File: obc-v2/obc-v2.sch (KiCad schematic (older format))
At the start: 12 parts

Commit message: obc-v2: Update microcontroller power circuitry
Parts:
- removed C? (x2): 15pF, symbol Device:C
- removed R?: R_US, symbol Device:R_US
- added FB?: Ferrite_Bead, symbol Device:Ferrite_Bead
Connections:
- net labels removed: AIN1, AIN2, AIN3, INT3, INT4, VOUT, XOUT
- wire segments 40 -> 32
- no-connect marks 0 -> 2
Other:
- moved on the sheet: C?

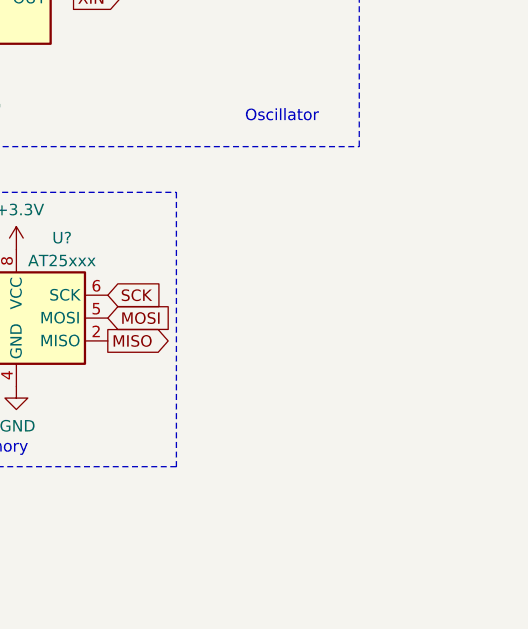
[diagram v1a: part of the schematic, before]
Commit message: obc-v2: Add BMI088 symbol
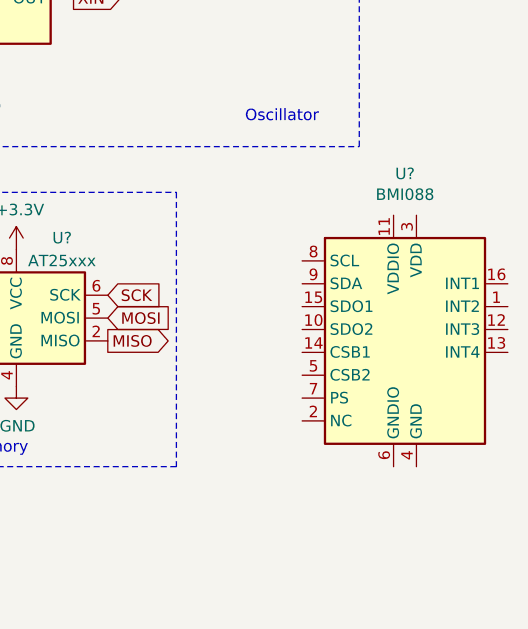
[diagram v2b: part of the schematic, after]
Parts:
- added U?: BMI088, Package_LGA:Bosch_LGA-14_3x2.5mm_P0.5mm, symbol bmi088:BMI088
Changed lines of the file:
@@
 Wire Notes Line
 	4150 800  4150 4550
+$Comp
+L bmi088:BMI088 U?
+U 1 1 6126D77D
+P 7250 2700
+F 0 "U?" H 7200 3281 50  0000 C CNN
+F 1 "BMI088" H 7200 3190 50  0000 C CNN
+F 2 "Package_LGA:Bosch_LGA-14_3x2.5mm_P0.5mm" H 7250 2700 50  0001 C CNN
+F 3 "https://ae-bst.resource.bosch.com/media/_tech/media/datasheets/BST-BMI160-DS000.pdf" H 6550 3550 50  0001 C CNN
+	1    7250 2700
+	1    0    0    -1
+$EndComp
 $EndSCHEMATC

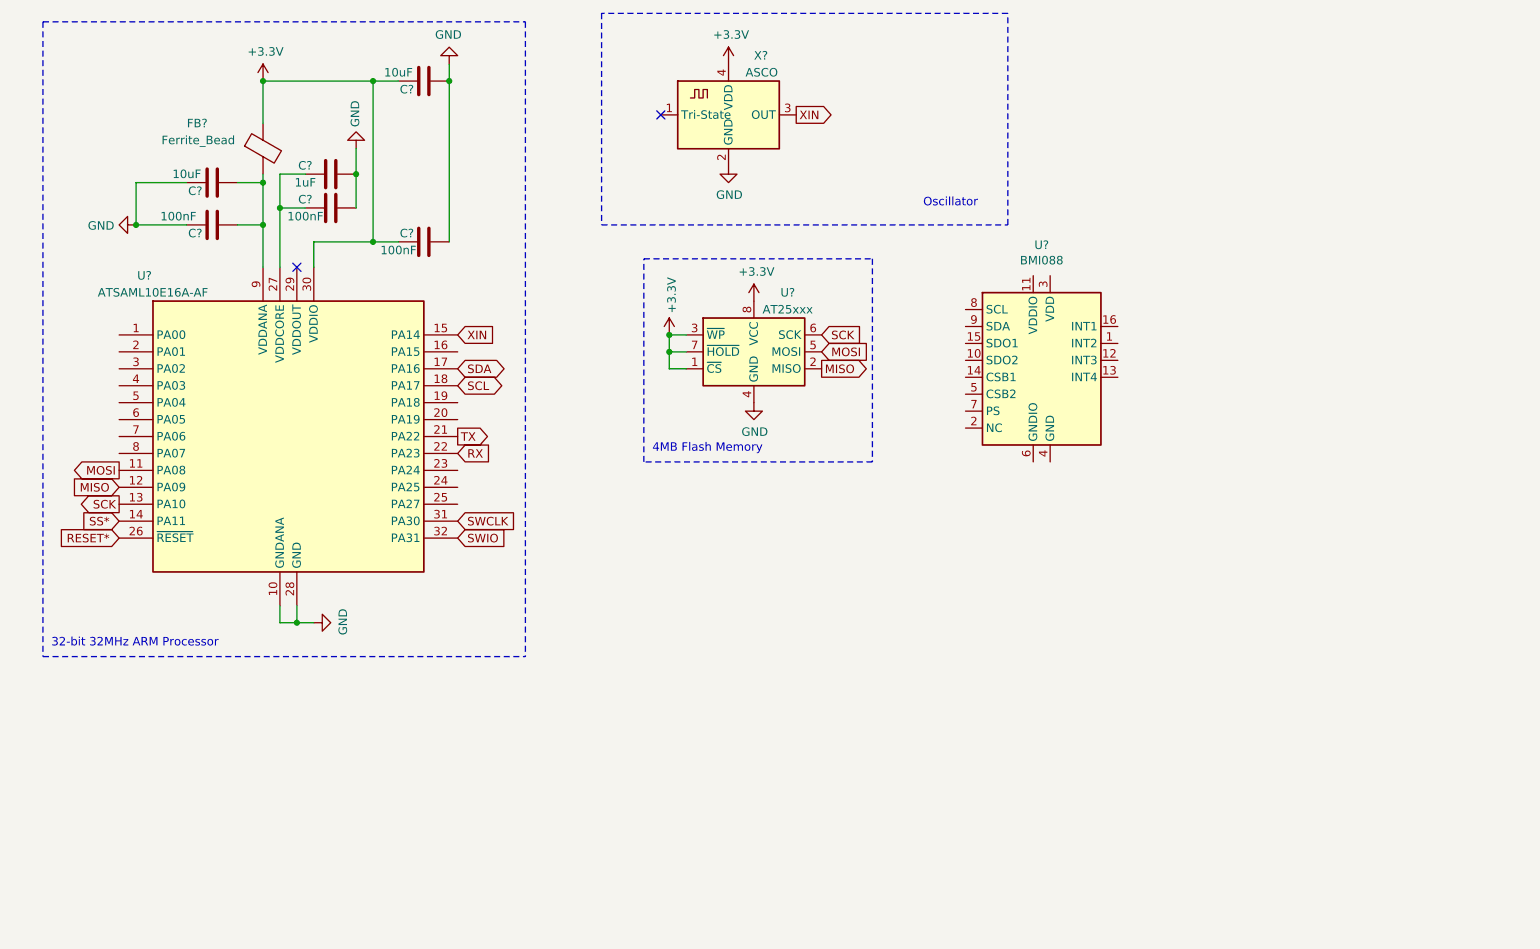
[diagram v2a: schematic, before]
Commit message: obc-v2: Add IMU
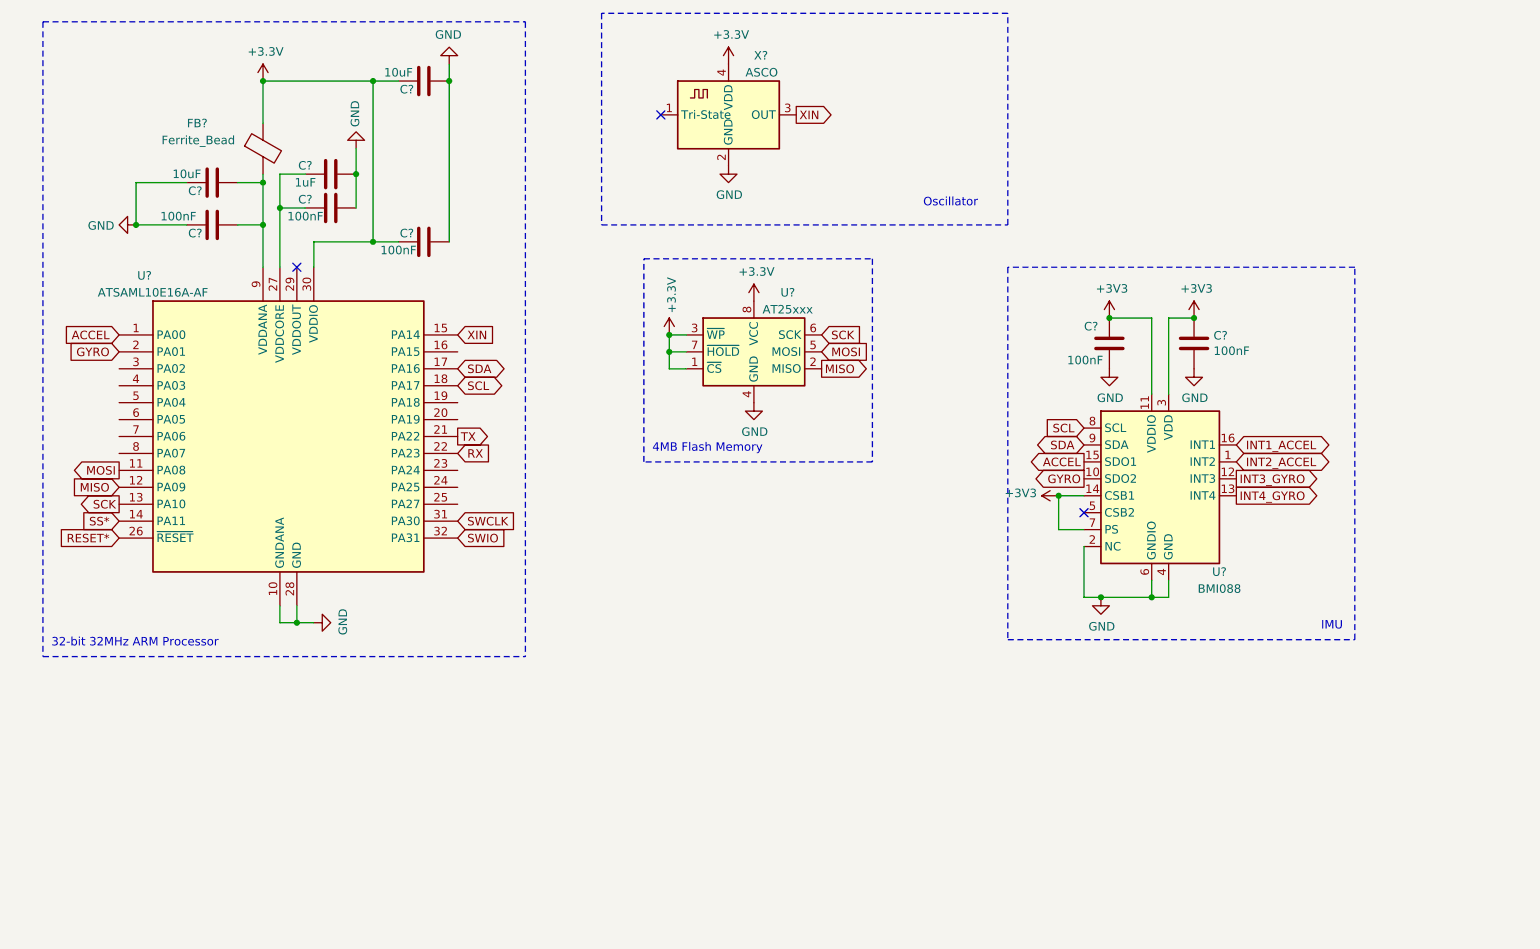
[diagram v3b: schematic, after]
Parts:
- added C? (x2): 100nF, symbol Device:C
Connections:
- net +3V3: now also U?.11 (VDDIO), U?.14 (CSB1), U?.3 (VDD), U?.7 (PS), C?.1, C?.1
- net GND: now also U?.2 (NC), U?.4 (GND), U?.6 (GNDIO), C?.2, C?.2
- net SCL: now also U?.8 (SCL)
- net SDA: now also U?.9 (SDA)
- net ACCEL: now reaches U?.1 (PA00)
- net ACCEL: now also U?.15 (SDO1)
- net GYRO: now reaches U?.2 (PA01)
- net GYRO: now also U?.10 (SDO2)
- net INT2_ACCEL: now reaches U?.1 (INT2)
- net INT3_GYRO: now reaches U?.12 (INT3)
- net INT4_GYRO: now reaches U?.13 (INT4)
- net INT1_ACCEL: now reaches U?.16 (INT1)
- no-connect marks 2 -> 3
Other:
- note added: "IMU"
- moved on the sheet: U?
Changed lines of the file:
@@
 Wire Notes Line
 	4150 800  4150 4550
+Text GLabel 7450 3300 0    50   BiDi ~ 0
+SDA
+Text GLabel 7450 3200 0    50   Input ~ 0
+SCL
+Text GLabel 7450 3400 0    50   Output ~ 0
+ACCEL
+Text GLabel 7450 3500 0    50   Output ~ 0
+GYRO
+NoConn ~ 7450 3700
+$Comp
+L power:GND #PWR?
+U 1 1 612718CF
+P 7550 4200
+F 0 "#PWR?" H 7550 3950 50  0001 C CNN
+F 1 "GND" H 7555 4027 50  0000 C CNN
+F 2 "" H 7550 4200 50  0001 C CNN
+F 3 "" H 7550 4200 50  0001 C CNN
+	1    7550 4200
+	1    0    0    -1
+$EndComp
+Wire Wire Line
+	7450 3900 7450 4200
+Wire Wire Line
+	7450 4200 7550 4200
+Wire Wire Line
+	7950 4200 7950 4100
+Connection ~ 7550 4200
+Wire Wire Line
+	7550 4200 7850 4200
+Wire Wire Line
+	7850 4100 7850 4200
+Connection ~ 7850 4200
+Wire Wire Line
+	7850 4200 7950 4200
+$Comp
+L power:+3V3 #PWR?
+U 1 1 61272ED0
+P 7300 3600
+F 0 "#PWR?" H 7300 3450 50  0001 C CNN
+F 1 "+3V3" V 7315 3728 50  0000 L CNN
+F 2 "" H 7300 3600 50  0001 C CNN
+F 3 "" H 7300 3600 50  0001 C CNN
+	1    7300 3600
+	0    -1   -1   0
+$EndComp
+Wire Wire Line
+	7450 3600 7300 3600
+Wire Wire Line
+	7300 3600 7300 3800
+Wire Wire Line
+	7300 3800 7450 3800
+Connection ~ 7300 3600
+Text GLabel 8350 3300 2    50   BiDi ~ 0
+INT1_ACCEL
+Text GLabel 8350 3400 2    50   BiDi ~ 0
+INT2_ACCEL
 $Comp
 L bmi088:BMI088 U?
 U 1 1 6126D77D
-P 7250 2700
-F 0 "U?" H 7200 3281 50  0000 C CNN
-F 1 "BMI088" H 7200 3190 50  0000 C CNN
-F 2 "Package_LGA:Bosch_LGA-14_3x2.5mm_P0.5mm" H 7250 2700 50  0001 C CNN
-F 3 "https://ae-bst.resource.bosch.com/media/_tech/media/datasheets/BST-BMI160-DS000.pdf" H 6550 3550 50  0001 C CNN
-	1    7250 2700
+P 7950 3400
+F 0 "U?" H 8250 2750 50  0000 C CNN
+F 1 "BMI088" H 8250 2650 50  0000 C CNN
+F 2 "Package_LGA:Bosch_LGA-14_3x2.5mm_P0.5mm" H 7950 3400 50  0001 C CNN
+F 3 "https://ae-bst.resource.bosch.com/media/_tech/media/datasheets/BST-BMI160-DS000.pdf" H 7250 4250 50  0001 C CNN
+	1    7950 3400
 	1    0    0    -1
 $EndComp
+Text GLabel 8350 3500 2    50   Output ~ 0
+INT3_GYRO
+Text GLabel 8350 3600 2    50   Output ~ 0
+INT4_GYRO
+$Comp
+L power:+3V3 #PWR?
+U 1 1 61277D25
+P 7600 2550
+F 0 "#PWR?" H 7600 2400 50  0001 C CNN
+F 1 "+3V3" H 7615 2723 50  0000 C CNN
+F 2 "" H 7600 2550 50  0001 C CNN
+F 3 "" H 7600 2550 50  0001 C CNN
+	1    7600 2550
+	1    0    0    -1
+$EndComp
+$Comp
+L power:+3V3 #PWR?
+U 1 1 612781FE
+P 8100 2550
+F 0 "#PWR?" H 8100 2400 50  0001 C CNN
+F 1 "+3V3" H 8115 2723 50  0000 C CNN
+F 2 "" H 8100 2550 50  0001 C CNN
+F 3 "" H 8100 2550 50  0001 C CNN
+	1    8100 2550
+	1    0    0    -1
+$EndComp
+$Comp
+L Device:C C?
+U 1 1 612799A4
+P 7600 2700
+F 0 "C?" H 7450 2800 50  0000 L CNN
+F 1 "100nF" H 7350 2600 50  0000 L CNN
+F 2 "" H 7638 2550 50  0001 C CNN
+F 3 "~" H 7600 2700 50  0001 C CNN
+	1    7600 2700
+	1    0    0    -1
+$EndComp
+$Comp
+L Device:C C?
+U 1 1 6127A006
+P 8100 2700
+F 0 "C?" H 8215 2746 50  0000 L CNN
+F 1 "100nF" H 8215 2655 50  0000 L CNN
+F 2 "" H 8138 2550 50  0001 C CNN
+F 3 "~" H 8100 2700 50  0001 C CNN
+	1    8100 2700
+	1    0    0    -1
+$EndComp
+$Comp
+L power:GND #PWR?
+U 1 1 6127AE14
+P 7600 2850
+F 0 "#PWR?" H 7600 2600 50  0001 C CNN
+F 1 "GND" H 7605 2677 50  0000 C CNN
+F 2 "" H 7600 2850 50  0001 C CNN
+F 3 "" H 7600 2850 50  0001 C CNN
+	1    7600 2850
+	1    0    0    -1
+$EndComp
+$Comp
+L power:GND #PWR?
+U 1 1 6127B677
+P 8100 2850
+F 0 "#PWR?" H 8100 2600 50  0001 C CNN
+F 1 "GND" H 8105 2677 50  0000 C CNN
+F 2 "" H 8100 2850 50  0001 C CNN
+F 3 "" H 8100 2850 50  0001 C CNN
+	1    8100 2850
+	1    0    0    -1
+$EndComp
+Wire Wire Line
+	7600 2550 7850 2550
+Wire Wire Line
+	7850 2550 7850 3000
+Connection ~ 7600 2550
+Wire Wire Line
+	8100 2550 7950 2550
+Wire Wire Line
+	7950 2550 7950 3000
+Connection ~ 8100 2550
+Wire Notes Line
+	7000 2250 7000 4450
+Wire Notes Line
+	7000 4450 9050 4450
+Wire Notes Line
+	9050 4450 9050 2250
+Wire Notes Line
+	9050 2250 7000 2250
+Text Notes 8850 4400 0    50   ~ 0
+IMU
+Text GLabel 1750 2650 0    50   Input ~ 0
+ACCEL
+Text GLabel 1750 2750 0    50   Input ~ 0
+GYRO
 $EndSCHEMATC

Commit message: obc-v2: Add IMU interrupt and memory chip select connections
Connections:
- net +3V3: now also U?.10 (SDO2), U?.15 (SDO1); no longer U?.1 (~CS)
- net INT1_ACCEL: now also U?.1 (PA00)
- net INT2_ACCEL: now also U?.2 (PA01)
- net INT3_GYRO: now also U?.3 (PA02)
- net INT4_GYRO: now also U?.4 (PA03)
- net SS*: now also U?.1 (~CS)
- removed net ACCEL: U?.1 (PA00), U?.15 (SDO1)
- removed net GYRO: U?.10 (SDO2), U?.2 (PA01)
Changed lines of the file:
@@
 Text GLabel 1750 3650 0    50   Output ~ 0
 SCK
-Text GLabel 1750 3750 0    50   Input ~ 0
+Text GLabel 1750 3750 0    50   Output ~ 0
 SS*
 Text GLabel 1750 3850 0    50   Input ~ 0
@@
 RX
 $Comp
-L MCU_Microchip_SAML_NEW:ATSAML10E16A-AF U?
-U 1 1 61106D2F
-P 2750 3250
-F 0 "U?" H 1900 4200 50  0000 C CNN
-F 1 "ATSAML10E16A-AF" H 1950 4100 50  0000 C CNN
-F 2 "Package_QFP:TQFP-32_7x7mm_P0.8mm" H 3750 4150 50  0001 C CNN
-F 3 "https://ww1.microchip.com/downloads/en/DeviceDoc/SAM-L10L11-Family-DataSheet-DS60001513F.pdf" H 2750 3250 50  0001 C CNN
-	1    2750 3250
-	1    0    0    -1
-$EndComp
-$Comp
 L power:+3.3V #PWR?
 U 1 1 61149F54
@@
 	1    0    0    -1
 $EndComp
-Wire Notes Line
-	1300 800  4150 800
 $Comp
 L power:GND #PWR?
@@
 	5000 2650 5000 2750
 Wire Wire Line
-	5000 2850 5100 2850
-Wire Wire Line
 	5000 2750 5100 2750
-Connection ~ 5000 2750
-Wire Wire Line
-	5000 2750 5000 2850
 Wire Wire Line
 	5000 2650 5100 2650
@@
 	2800 4250 2800 4350
 Wire Notes Line
-	1300 800  1300 4550
-Wire Notes Line
-	1300 4550 4150 4550
+	1200 800  1200 4550
 Wire Notes Line
 	4150 800  4150 4550
@@
 Text GLabel 7450 3200 0    50   Input ~ 0
 SCL
-Text GLabel 7450 3400 0    50   Output ~ 0
-ACCEL
-Text GLabel 7450 3500 0    50   Output ~ 0
-GYRO
 NoConn ~ 7450 3700
 $Comp
@@
 	7300 3800 7450 3800
 Connection ~ 7300 3600
-Text GLabel 8350 3300 2    50   BiDi ~ 0
+Text GLabel 8350 3300 2    50   Output ~ 0
 INT1_ACCEL
-Text GLabel 8350 3400 2    50   BiDi ~ 0
+Text GLabel 8350 3400 2    50   Output ~ 0
 INT2_ACCEL
 $Comp
@@
 Connection ~ 8100 2550
 Wire Notes Line
-	7000 2250 7000 4450
-Wire Notes Line
-	7000 4450 9050 4450
+	6900 2250 6900 4450
 Wire Notes Line
 	9050 4450 9050 2250
-Wire Notes Line
-	9050 2250 7000 2250
 Text Notes 8850 4400 0    50   ~ 0
 IMU
+Wire Wire Line
+	7450 3400 7300 3400
+Wire Wire Line
+	7450 3500 7300 3500
+Wire Wire Line
+	7300 3400 7300 3500
+Connection ~ 7300 3500
+Wire Wire Line
+	7300 3500 7300 3600
 Text GLabel 1750 2650 0    50   Input ~ 0
-ACCEL
+INT1_ACCEL
 Text GLabel 1750 2750 0    50   Input ~ 0
-GYRO
+INT2_ACCEL
+Text GLabel 1750 2850 0    50   Input ~ 0
+INT3_GYRO
+Text GLabel 1750 2950 0    50   Input ~ 0
+INT4_GYRO
+$Comp
+L MCU_Microchip_SAML_NEW:ATSAML10E16A-AF U?
+U 1 1 61106D2F
+P 2750 3250
+F 0 "U?" H 1900 4200 50  0000 C CNN
+F 1 "ATSAML10E16A-AF" H 1950 4100 50  0000 C CNN
+F 2 "Package_QFP:TQFP-32_7x7mm_P0.8mm" H 3750 4150 50  0001 C CNN
+F 3 "https://ww1.microchip.com/downloads/en/DeviceDoc/SAM-L10L11-Family-DataSheet-DS60001513F.pdf" H 2750 3250 50  0001 C CNN
+	1    2750 3250
+	1    0    0    -1
+$EndComp
+Wire Notes Line
+	1200 4550 4150 4550
+Wire Notes Line
+	1200 800  4150 800
+Text GLabel 5100 2850 0    50   Input ~ 0
+SS*
+Wire Notes Line
+	6900 4450 9050 4450
+Wire Notes Line
+	6900 2250 9050 2250
 $EndSCHEMATC

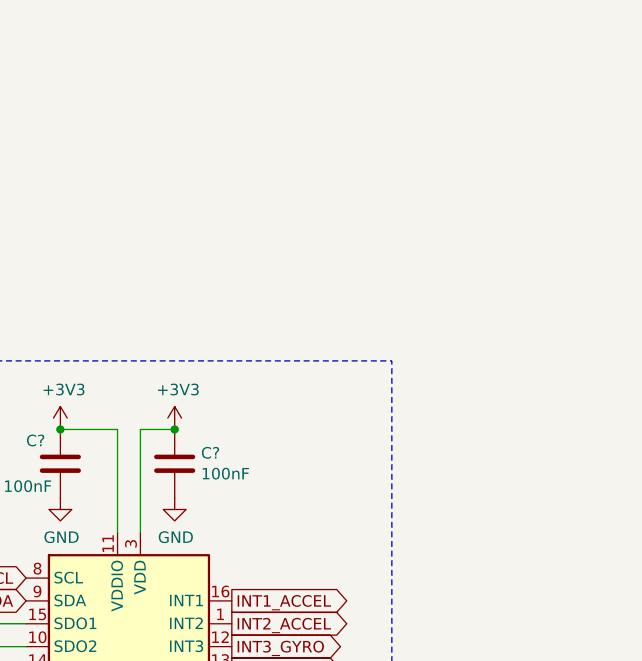
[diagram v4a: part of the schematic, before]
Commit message: obc-v2: Add barometer
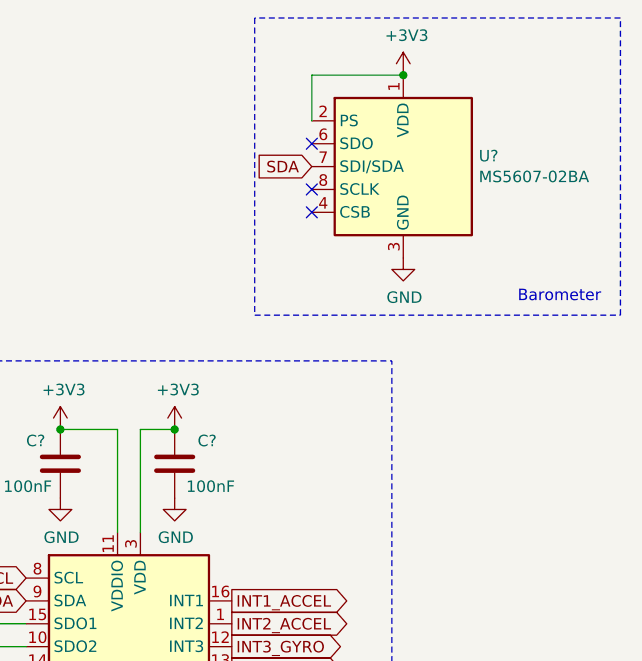
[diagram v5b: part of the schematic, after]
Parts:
- added U?: MS5607-02BA, Package_LGA:LGA-8_3x5mm_P1.25mm, symbol Sensor_Pressure:MS5607-02BA
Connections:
- net +3V3: now also U?.1 (VDD), U?.2 (PS)
- net GND: now also U?.3 (GND)
- net SDA: now also U?.7 (SDI/SDA)
- new net: U?.4 (CSB), U?.5 (CSB)
- no-connect marks 3 -> 6
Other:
- note added: "Barometer"
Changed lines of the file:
@@
 U 1 1 6127A006
 P 8100 2700
-F 0 "C?" H 8215 2746 50  0000 L CNN
-F 1 "100nF" H 8215 2655 50  0000 L CNN
+F 0 "C?" H 8200 2800 50  0000 L CNN
+F 1 "100nF" H 8150 2600 50  0000 L CNN
 F 2 "" H 8138 2550 50  0001 C CNN
 F 3 "~" H 8100 2700 50  0001 C CNN
@@
 Wire Notes Line
 	6900 2250 9050 2250
+$Comp
+L Sensor_Pressure:MS5607-02BA U?
+U 1 1 61291CE6
+P 9100 1400
+F 0 "U?" H 9430 1446 50  0000 L CNN
+F 1 "MS5607-02BA" H 9430 1355 50  0000 L CNN
+F 2 "Package_LGA:LGA-8_3x5mm_P1.25mm" H 9100 1400 50  0001 C CNN
+F 3 "https://www.te.com/commerce/DocumentDelivery/DDEController?Action=showdoc&DocId=Data+Sheet%7FMS5607-02BA03%7FB2%7Fpdf%7FEnglish%7FENG_DS_MS5607-02BA03_B2.pdf%7FCAT-BLPS0035" H 9100 1400 50  0001 C CNN
+	1    9100 1400
+	1    0    0    -1
+$EndComp
+$Comp
+L power:GND #PWR?
+U 1 1 61292644
+P 9100 1800
+F 0 "#PWR?" H 9100 1550 50  0001 C CNN
+F 1 "GND" H 9105 1627 50  0000 C CNN
+F 2 "" H 9100 1800 50  0001 C CNN
+F 3 "" H 9100 1800 50  0001 C CNN
+	1    9100 1800
+	1    0    0    -1
+$EndComp
+$Comp
+L power:+3V3 #PWR?
+U 1 1 61292BCA
+P 9100 1000
+F 0 "#PWR?" H 9100 850 50  0001 C CNN
+F 1 "+3V3" H 9115 1173 50  0000 C CNN
+F 2 "" H 9100 1000 50  0001 C CNN
+F 3 "" H 9100 1000 50  0001 C CNN
+	1    9100 1000
+	1    0    0    -1
+$EndComp
+Wire Wire Line
+	8700 1200 8700 1000
+Wire Wire Line
+	8700 1000 9100 1000
+Connection ~ 9100 1000
+Text GLabel 8700 1400 0    50   Input ~ 0
+SDA
+NoConn ~ 8700 1300
+NoConn ~ 8700 1500
+NoConn ~ 8700 1600
+Wire Notes Line
+	10050 2050 10050 750
+Wire Notes Line
+	10050 750  8450 750
+Wire Notes Line
+	8450 750  8450 2050
+Wire Notes Line
+	8450 2050 10050 2050
+Text Notes 9600 2000 0    50   ~ 0
+Barometer
 $EndSCHEMATC

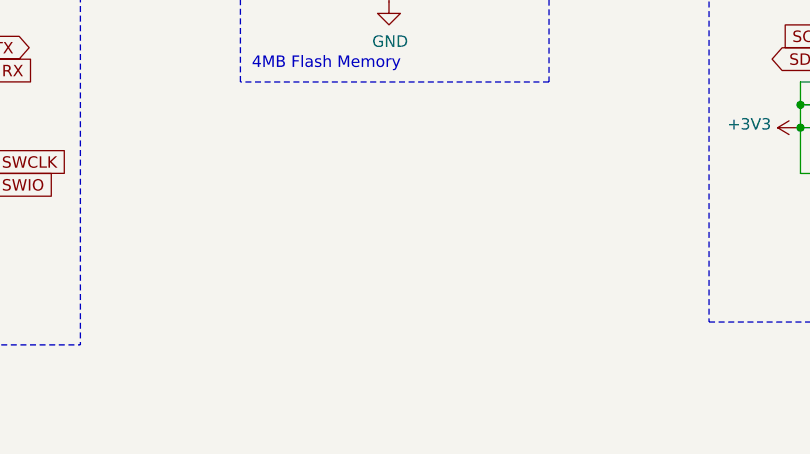
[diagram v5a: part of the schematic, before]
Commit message: Add 1-wire interface for thermal sensors
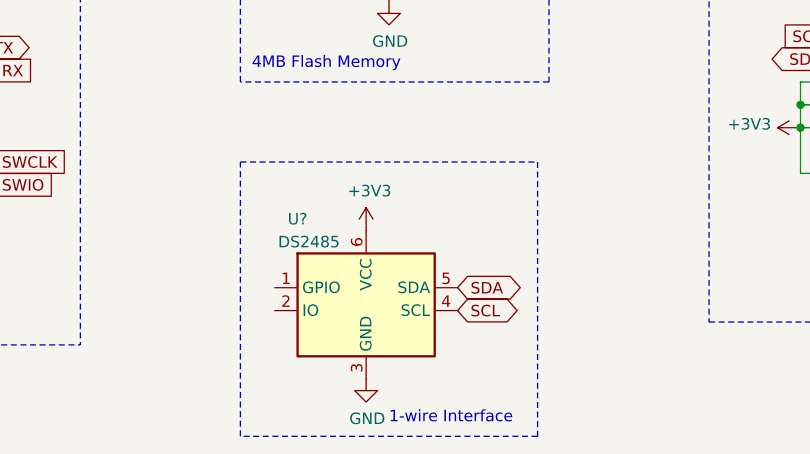
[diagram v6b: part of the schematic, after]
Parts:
- added U?: DS2485, symbol DS2845:DS2485
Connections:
- net +3V3: now also U?.6 (VCC)
- net GND: now also U?.3 (GND)
- net SCL: now also U?.4 (SCL)
- net SDA: now also U?.5 (SDA)
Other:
- note added: "1-wire Interface"
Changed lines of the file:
@@
 Text Notes 9600 2000 0    50   ~ 0
 Barometer
+$Comp
+L DS2845:DS2485 U?
+U 1 1 6129E0CF
+P 5400 4350
+F 0 "U?" H 5100 4700 50  0000 C CNN
+F 1 "DS2485" H 5150 4600 50  0000 C CNN
+F 2 "" H 5450 4500 50  0001 C CNN
+F 3 "" H 5450 4500 50  0001 C CNN
+	1    5400 4350
+	1    0    0    -1
+$EndComp
+$Comp
+L power:GND #PWR?
+U 1 1 6129E849
+P 5400 4700
+F 0 "#PWR?" H 5400 4450 50  0001 C CNN
+F 1 "GND" H 5405 4527 50  0000 C CNN
+F 2 "" H 5400 4700 50  0001 C CNN
+F 3 "" H 5400 4700 50  0001 C CNN
+	1    5400 4700
+	1    0    0    -1
+$EndComp
+$Comp
+L power:+3V3 #PWR?
+U 1 1 6129EE3F
+P 5400 4050
+F 0 "#PWR?" H 5400 3900 50  0001 C CNN
+F 1 "+3V3" H 5415 4223 50  0000 C CNN
+F 2 "" H 5400 4050 50  0001 C CNN
+F 3 "" H 5400 4050 50  0001 C CNN
+	1    5400 4050
+	1    0    0    -1
+$EndComp
+Text GLabel 5800 4300 2    50   BiDi ~ 0
+SDA
+Text GLabel 5800 4400 2    50   BiDi ~ 0
+SCL
+Wire Notes Line
+	4850 3750 6150 3750
+Wire Notes Line
+	6150 3750 6150 4950
+Wire Notes Line
+	6150 4950 4850 4950
+Wire Notes Line
+	4850 4950 4850 3750
+Text Notes 5500 4900 0    50   ~ 0
+1-wire Interface
 $EndSCHEMATC
